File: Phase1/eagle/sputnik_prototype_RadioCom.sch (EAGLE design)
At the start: 98 parts, among them X1 332-44, Y1 32MHz

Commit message: Added more LEDs, filled in LNA values except one inductor which I still need to figure out
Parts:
- added LED7, LED8: (no value), psas_c3_team05:LED-0603
- added R11, R12: 1k, rcl_custom:R-US_0603-B-NOSILK
- C23: value (none) -> 1nF
- C24: value (none) -> 10nF
- C43: value (none) -> 100uF
- L8: value (none) -> 150nH
- R1: value (none) -> 250
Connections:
- removed net N$28: LED5.A
- new net N$21: LED7.K, R11.2
- new net N$33: LED8.K, R12.2
- net GND: now also R11.1, R12.1
- net PTC1: now also LED5.A
- net PTC3: now also LED7.A
- net PTC4: now also LED8.A
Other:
- note added: "TODO: FIGURE OUT VALUE FOR L7"
- note removed: "TODO: FIGURE OUT VALUES FOR LNA"
- moved on the sheet: JP2, LED1, LED4, LED5, LED6, R10, R4, R8, R9

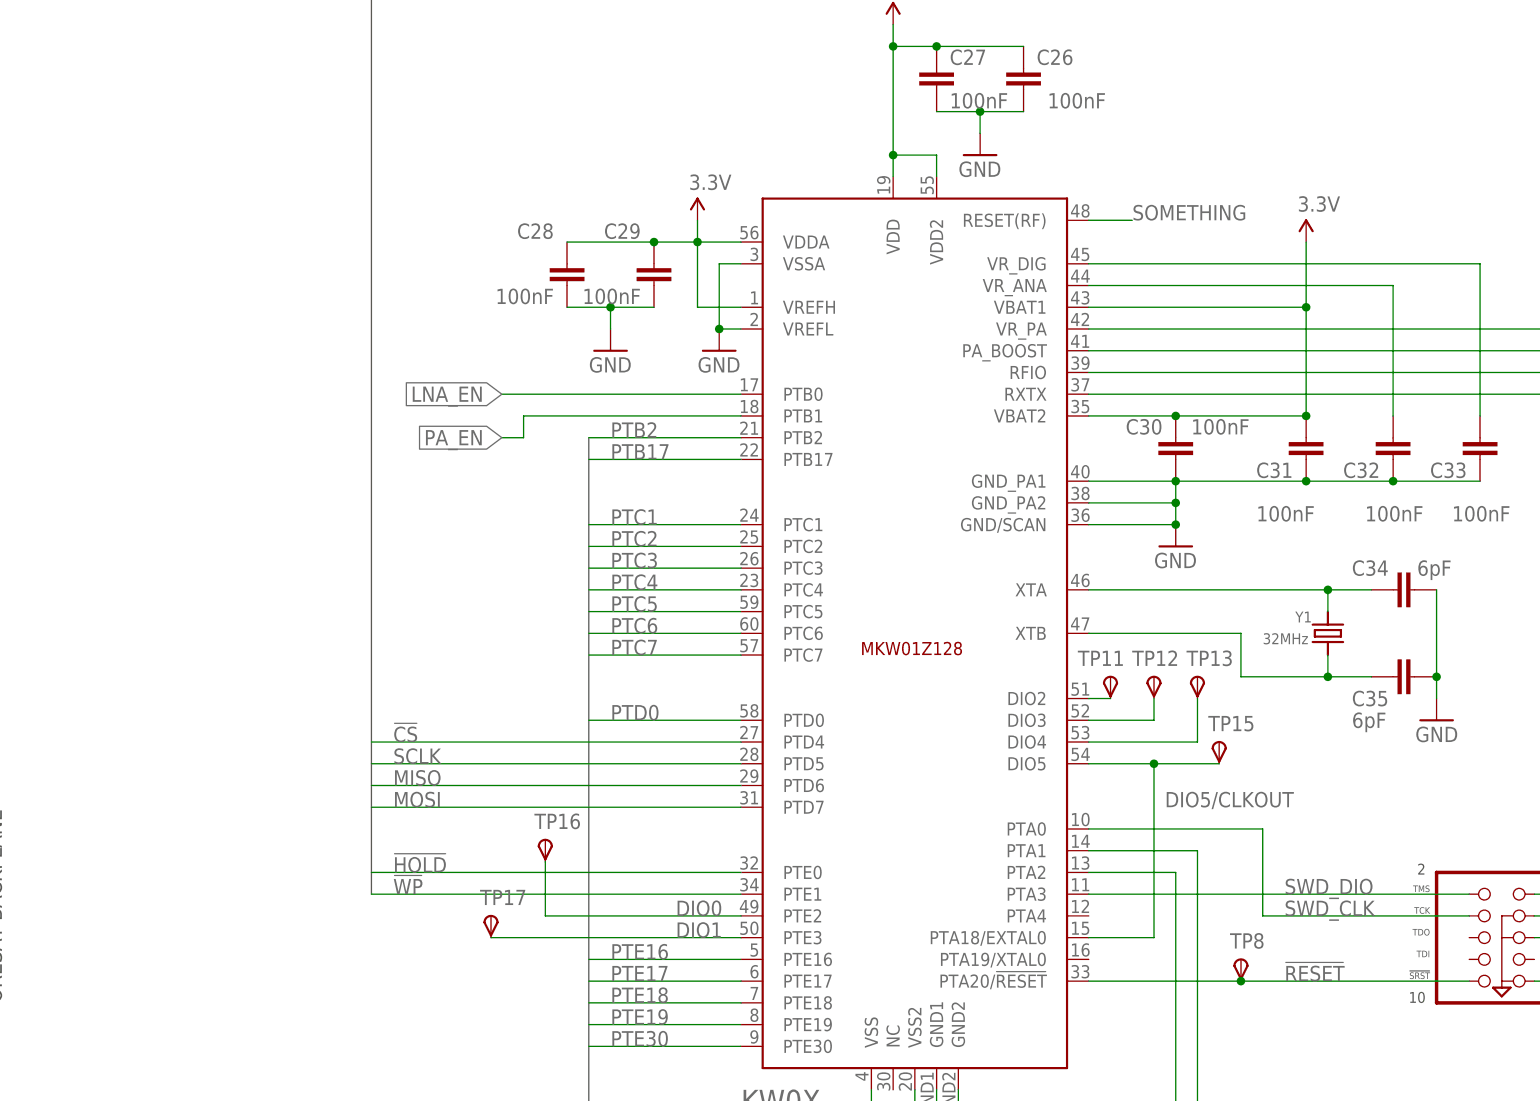
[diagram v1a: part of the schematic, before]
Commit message: Added RESET (RF) line to PTE2 GPIO. Waiting on LNA component values from MAACOM.
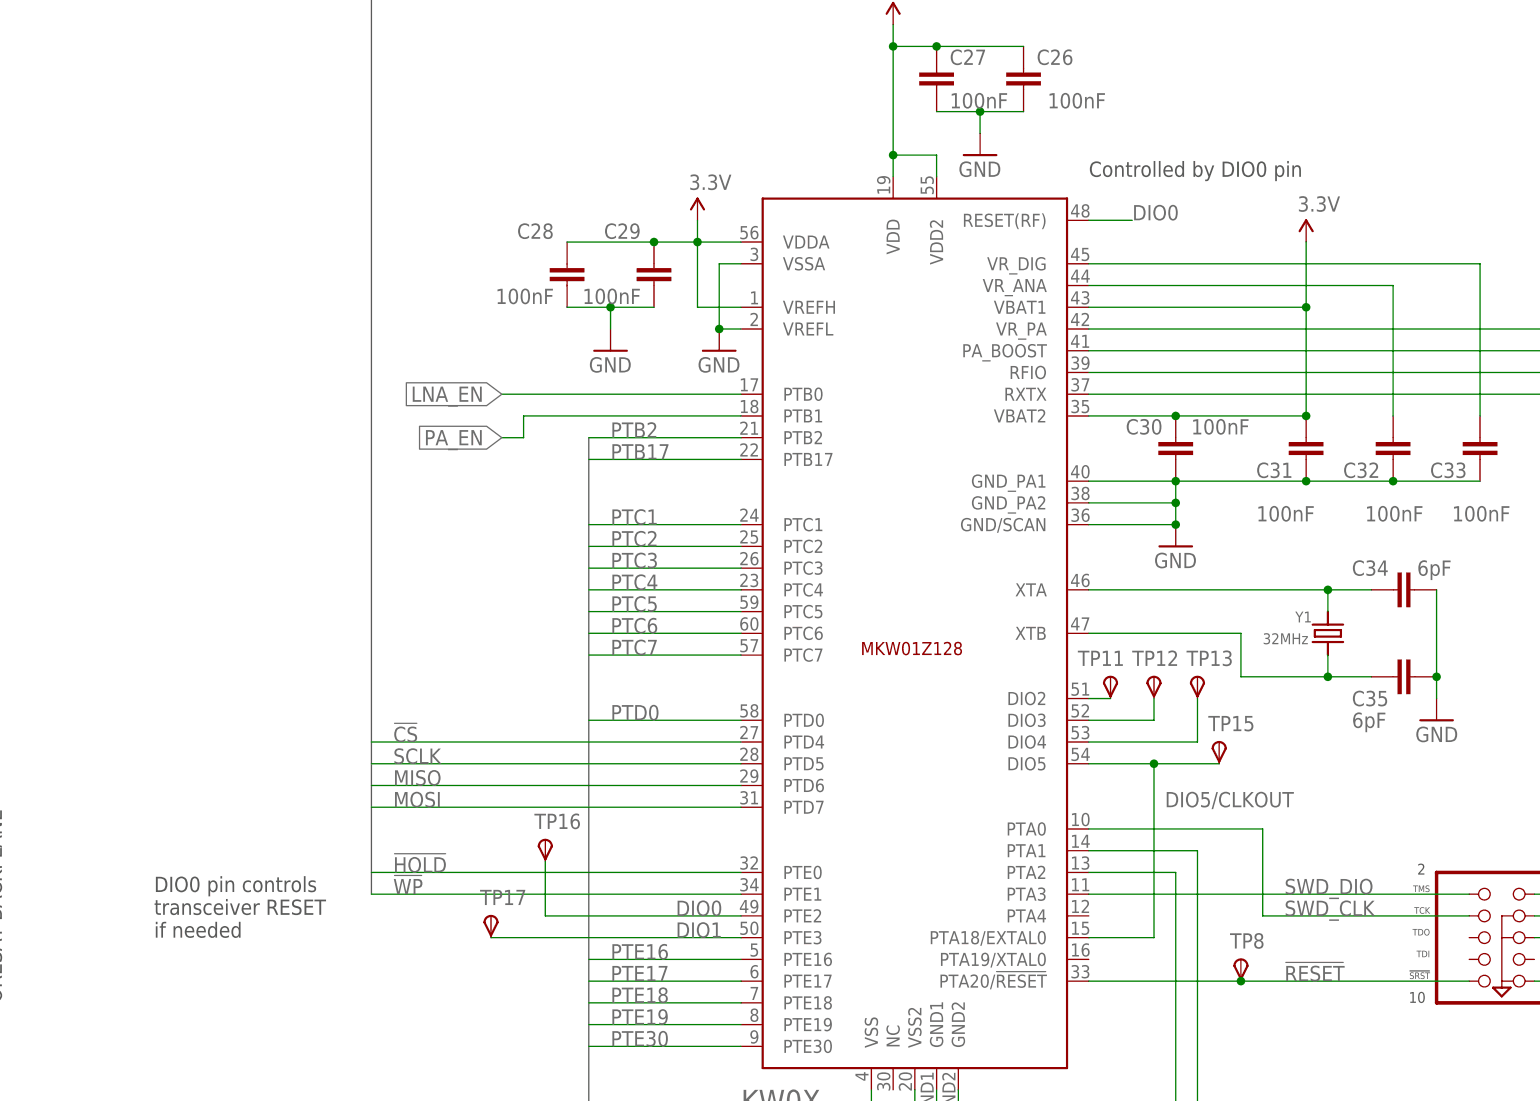
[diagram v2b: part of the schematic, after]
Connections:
- removed net SOMETHING: KW0X.RESET(RF)
- net DIO0: now also KW0X.RESET(RF)
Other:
- note added: "Controlled by DIO0 pin"
- note added: "DIO0 pin controls transceiver RESET if needed"
- note removed: "DOES !RESET NEED A PULL-UP?!"
- note removed: "FIXME!!!!"
- note removed: "TODO: -Make footprint for 22pin (83B-44PA-2DS(71)-ND) (H123075-ND)"
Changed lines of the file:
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@@
 <wire x1="83.82" y1="279.4" x2="139.7" y2="279.4" width="0.1524" layer="97" style="longdash"/>
 <wire x1="139.7" y1="279.4" x2="139.7" y2="322.58" width="0.1524" layer="97" style="longdash"/>
-<text x="104.14" y="66.04" size="1.778" layer="100">TODO:
--Make footprint for 22pin (83B-44PA-2DS(71)-ND)
-(H123075-ND)</text>
 <wire x1="314.96" y1="231.14" x2="241.3" y2="231.14" width="0.1524" layer="97" style="longdash"/>
 <wire x1="309.88" y1="99.06" x2="340.36" y2="99.06" width="0.1524" layer="97" style="longdash"/>
@@
 <wire x1="309.88" y1="78.74" x2="309.88" y2="99.06" width="0.1524" layer="97" style="longdash"/>
 <text x="312.42" y="96.52" size="1.778" layer="97">RF/DC GND connection</text>
-<text x="142.24" y="250.19" size="1.778" layer="100">FIXME!!!!</text>
-<text x="152.4" y="147.32" size="1.778" layer="100">DOES !RESET NEED
-A PULL-UP?!</text>
 <text x="213.36" y="86.36" size="1.778" layer="97">Debug interface</text>
 <wire x1="261.62" y1="2.54" x2="160.02" y2="2.54" width="0.1524" layer="97" style="longdash"/>
@@
 <text x="223.52" y="49.53" size="1.778" layer="97" rot="R90">Placed by access edge</text>
 <text x="7.62" y="154.94" size="1.778" layer="97" rot="R90">ORESAT BACKPLANE</text>
+<text x="134.62" y="251.46" size="1.778" layer="97">Controlled by DIO0 pin</text>
+<text x="25.4" y="162.56" size="1.778" layer="97">DIO0 pin controls
+transceiver RESET
+if needed</text>
 </plain>
 <instances>
@@
 </segment>
 </net>
-<net name="SOMETHING" class="0">
-<segment>
-<pinref part="KW0X" gate="G$1" pin="RESET(RF)"/>
-<wire x1="134.62" y1="246.38" x2="139.7" y2="246.38" width="0.1524" layer="91"/>
-<label x="139.7" y="246.38" size="1.778" layer="95"/>
-</segment>
-</net>
 <net name="LNA_EN" class="0">
 <segment>
@@
 <label x="86.36" y="165.1" size="1.778" layer="95"/>
 </segment>
-</net>
+<segment>
+<pinref part="KW0X" gate="G$1" pin="RESET(RF)"/>
+<wire x1="134.62" y1="246.38" x2="139.7" y2="246.38" width="0.1524" layer="91"/>
+<label x="139.7" y="246.38" size="1.778" layer="95"/>
+</segment>
+</net>

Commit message: OCD fixes on SPI flash. Made single nets on GPIO that aren't connected. Made new connectors for OreSat connector and RF connector and added them. Updates to a library part for the outline. Made it 4 layers, because that's what it's gonna be. Ooo the excitement, this is starting to look like a thing. Still waiting for final placement data from Jeremy before the connectors can be finalized.
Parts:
- removed SMA: SMAJ716-ND, psas_c3_team05:SMAJ716-ND
- removed X1: 332-44, con-garry:332-44
- added CF1: ORESAT-CONNECTOR-40PIN, oresat-eagle:ORESAT-CONNECTOR-40PIN
- added CF2: CON-MCX-LINX, oresat-eagle:CON-MCX-LINX
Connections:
- net !WP renamed PTE1
- removed net 3.3V1: LED2.A
- removed net N$32: LED6.A
- new net PTE0: KW0X.PTE0
- net !HOLD: no longer KW0X.PTE0
- net 3.3V: no longer TP5.PP
- net GND: now also CF1.37, CF1.38, CF1.39, CF1.40, CF2.SHIELD; no longer SMA.OUTERCONDUCTOR, X1-21.S, X1-22.S
- net N$11: now also TP5.PP
- net N$30: now also CF2.CENTER; no longer SMA.CENTERCONDUCTOR
- net PTB17: now also CF1.2; no longer X1-4.S
- net PTB2: now also CF1.1; no longer X1-3.S
- net PTC1: now also CF1.3; no longer X1-5.S
- net PTC2: now also CF1.4, LED6.A; no longer X1-6.S
- net PTC3: now also CF1.5; no longer X1-7.S
- net PTC4: now also CF1.6; no longer X1-8.S
- net PTC5: now also CF1.7; no longer X1-9.S
- net PTC6: now also CF1.8; no longer X1-10.S
- net PTC7: now also CF1.9; no longer X1-11.S
- net PTD0: now also CF1.10; no longer X1-12.S
- net PTE16: now also CF1.11; no longer X1-13.S
- net PTE17: now also CF1.12; no longer X1-14.S
- net PTE18: now also CF1.13; no longer X1-15.S
- net PTE19: now also CF1.14; no longer X1-16.S
- net UART0_RX: now also CF1.17, CF1.18; no longer X1-19.S, X1-20.S
- net UART0_TX: now also CF1.15, CF1.16; no longer X1-17.S, X1-18.S
- net V+: now also CF1.33, CF1.34, CF1.35, CF1.36; no longer X1-1.S, X1-2.S
- net VBIAS: now also LED2.A
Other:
- note removed: "UART connection between KW0x and ATMega128 PTA1 = KW0x UART0 RX PTA2 = KW0x UART0 TX PE1 = ATMega128 UART0 TX PE0 = ATMega128 UART0 RX PE1 is connected to PTA1 PE0 is connected to PTA2"
- moved on the sheet: C39, C40, C41, R2, R3, R5, TP10, TP14, TP5, TP6, TP7

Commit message: Uhh.... I did stuff? Fixed something? I can't remember. Found another NC on the KW0x.
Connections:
- new net PTA19: KW0X.PTA19/XTAL0
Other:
- note removed: "Controlled by DIO0 pin"
- moved on the sheet: TP16, TP17
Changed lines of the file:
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@@
 <text x="223.52" y="49.53" size="1.778" layer="97" rot="R90">Placed by access edge</text>
 <text x="7.62" y="154.94" size="1.778" layer="97" rot="R90">ORESAT BACKPLANE</text>
-<text x="134.62" y="251.46" size="1.778" layer="97">Controlled by DIO0 pin</text>
-<text x="25.4" y="162.56" size="1.778" layer="97">DIO0 pin controls
+<text x="140.97" y="257.81" size="1.778" layer="97">DIO0 pin controls
 transceiver RESET
 if needed</text>
@@
 <attribute name="TP_SIGNAL_NAME" x="148.59" y="191.77" size="1.778" layer="97"/>
 </instance>
-<instance part="TP16" gate="G$1" x="71.12" y="173.99"/>
-<instance part="TP17" gate="G$1" x="64.77" y="165.1"/>
+<instance part="TP16" gate="G$1" x="71.12" y="167.64"/>
+<instance part="TP17" gate="G$1" x="66.04" y="170.18"/>
 <instance part="R2" gate="R" x="88.9" y="314.96" rot="R90"/>
 <instance part="P+8" gate="G$1" x="88.9" y="322.58" rot="MR0"/>
@@
 <net name="DIO0" class="0">
 <segment>
+<pinref part="KW0X" gate="G$1" pin="RESET(RF)"/>
+<wire x1="134.62" y1="246.38" x2="139.7" y2="246.38" width="0.1524" layer="91"/>
+<wire x1="139.7" y1="246.38" x2="139.7" y2="276.86" width="0.1524" layer="91"/>
+<wire x1="139.7" y1="276.86" x2="43.18" y2="276.86" width="0.1524" layer="91"/>
+<wire x1="43.18" y1="276.86" x2="43.18" y2="165.1" width="0.1524" layer="91"/>
 <pinref part="KW0X" gate="G$1" pin="PTE2"/>
 <pinref part="TP16" gate="G$1" pin="PP"/>
 <wire x1="93.98" y1="165.1" x2="71.12" y2="165.1" width="0.1524" layer="91"/>
-<wire x1="71.12" y1="165.1" x2="71.12" y2="171.45" width="0.1524" layer="91"/>
 <label x="86.36" y="165.1" size="1.778" layer="95"/>
-</segment>
-<segment>
-<pinref part="KW0X" gate="G$1" pin="RESET(RF)"/>
-<wire x1="134.62" y1="246.38" x2="139.7" y2="246.38" width="0.1524" layer="91"/>
-<label x="139.7" y="246.38" size="1.778" layer="95"/>
+<wire x1="43.18" y1="165.1" x2="71.12" y2="165.1" width="0.1524" layer="91"/>
+<junction x="71.12" y="165.1"/>
 </segment>
 </net>
@@
 <pinref part="TP17" gate="G$1" pin="PP"/>
 <pinref part="KW0X" gate="G$1" pin="PTE3"/>
-<wire x1="93.98" y1="162.56" x2="64.77" y2="162.56" width="0.1524" layer="91"/>
+<wire x1="93.98" y1="162.56" x2="66.04" y2="162.56" width="0.1524" layer="91"/>
+<wire x1="66.04" y1="162.56" x2="66.04" y2="167.64" width="0.1524" layer="91"/>
 <label x="86.36" y="162.56" size="1.778" layer="95"/>
 </segment>
@@
 </segment>
 </net>
+<net name="PTA19" class="0">
+<segment>
+<pinref part="KW0X" gate="G$1" pin="PTA19/XTAL0"/>
+<wire x1="134.62" y1="160.02" x2="142.24" y2="160.02" width="0.1524" layer="91"/>
+</segment>
+</net>

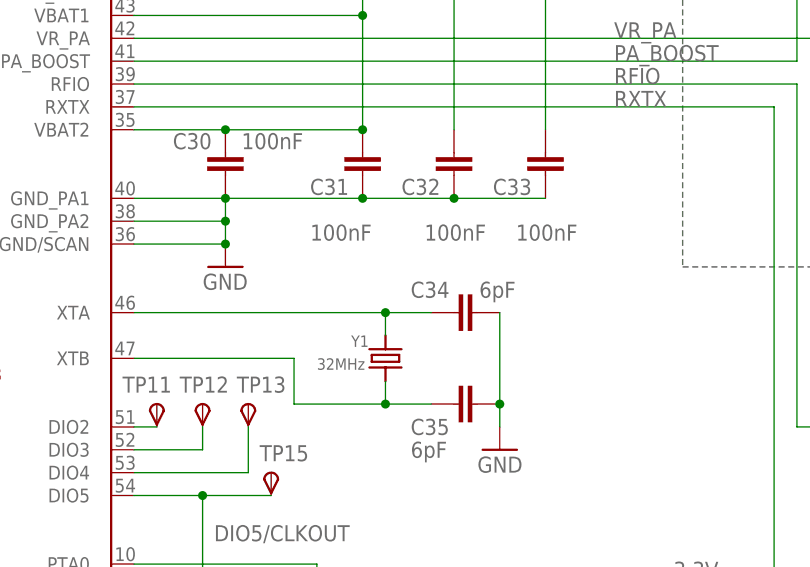
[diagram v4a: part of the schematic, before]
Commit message: Added crystal test point, started layout setup
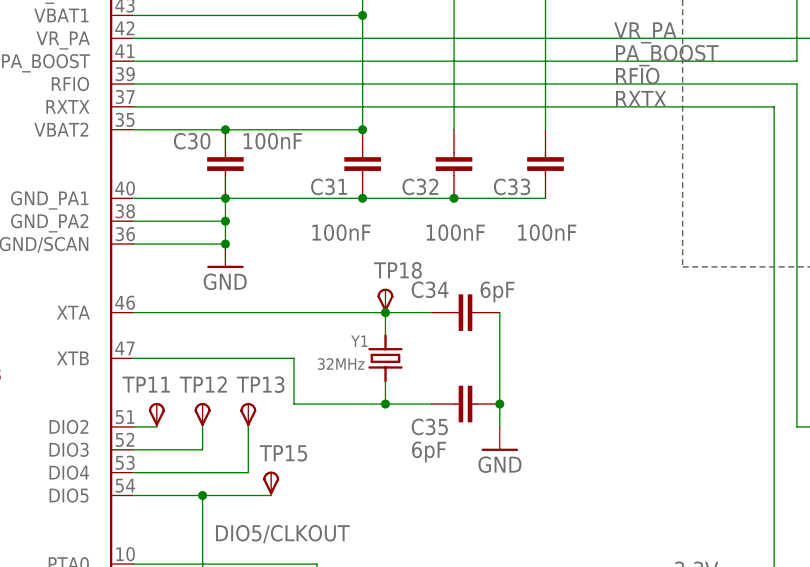
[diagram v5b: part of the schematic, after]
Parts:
- added TP18: TPSPAD1-13, testpad:TPSPAD1-13
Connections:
- net N$6: now also TP18.PP
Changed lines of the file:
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@@
 <?xml version="1.0" encoding="utf-8"?>
 <!DOCTYPE eagle SYSTEM "eagle.dtd">
-<eagle version="7.3.0">
+<eagle version="7.4.0">
 <drawing>
 <settings>
@@
 <setting verticaltext="up"/>
 </settings>
-<grid distance="0.05" unitdist="inch" unit="inch" style="lines" multiple="2" display="yes" altdistance="0.01" altunitdist="inch" altunit="inch"/>
+<grid distance="0.1" unitdist="inch" unit="inch" style="lines" multiple="1" display="no" altdistance="0.01" altunitdist="inch" altunit="inch"/>
 <layers>
 <layer number="1" name="Top" color="4" fill="1" visible="no" active="no"/>
@@
 <part name="CF1" library="oresat-eagle" deviceset="ORESAT-CONNECTOR-40PIN" device=""/>
 <part name="CF2" library="oresat-eagle" deviceset="CON-MCX-LINX" device=""/>
+<part name="TP18" library="testpad" deviceset="TPS" device="PAD1-13"/>
 </parts>
 <sheets>
@@
 <attribute name="VALUE" x="511.81" y="168.91" size="1.27" layer="95"/>
 </instance>
+<instance part="TP18" gate="G$1" x="162.56" y="205.74" smashed="yes">
+<attribute name="NAME" x="161.29" y="207.01" size="1.778" layer="95"/>
+<attribute name="TP_SIGNAL_NAME" x="163.83" y="204.47" size="1.778" layer="97"/>
+</instance>
 </instances>
 <busses>
@@
 <wire x1="162.56" y1="200.66" x2="162.56" y2="203.2" width="0.1524" layer="91"/>
 <junction x="162.56" y="203.2"/>
-</segment>
-</net>
+<pinref part="TP18" gate="G$1" pin="PP"/>
+</segment>
+</net>

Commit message: Poor Jake. It's like there's some crazy guy screwing with him every time he commits... oh, wait. Huh. Anyway. Updated board outline with keepouts. Moved connectors into position and locked. Added shield over LNA (how could this be a bad idea? maybe the PA could use a sheild too, but with heat sinking?). Uncrossed the streams: make sure your main RF lines never, ever dive through the board. That sucks, keep it to one layer. So I had to move the PA and LNA around. Still needs some cleanup, but it's OK. Put resistors for sensitive supplies by the supplies, so no stray low impedance leakage.
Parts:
- removed TP6, TP7: TPSPAD1-13, testpad:TPSPAD1-13
- added SH1: BMI-S-202-SHIELD, hw-laird-bmi-s-202:BMI-S-202-SHIELD
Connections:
- removed net N$26: LED5.K, R9.2
- removed net N$29: LED6.K, R10.2
- removed net N$33: LED8.K, R12.2
- new net N$23: LED8.A, R12.1
- new net V_LNA_FILTERED: LED2.A, R6.1
- new net V_PA_FILTERED: LED3.A, R7.1
- net 3.3V: now also R8.2; no longer LED4.A
- net GND: now also LED1.K, LED2.K, LED3.K, LED4.K, LED5.K, LED6.K, LED7.K, LED8.K, SH1.P$1; no longer R10.1, R11.1, R12.1, R4.1, R6.1, R7.1, R8.1, R9.1
- net LNA_IN: now also TRSWITCH.RF3; no longer TRSWITCH.RF2
- net N$14: now also LED1.A, R4.1; no longer LED1.K, R4.2
- net N$15: now also LED5.A, R9.1; no longer LED2.K, R6.2
- net N$2: now also TRSWITCH.RF2; no longer TRSWITCH.RF3
- net N$20: now also LED6.A, R10.1; no longer LED3.K, R7.2
- net N$21: now also LED7.A, R11.1; no longer LED7.K, R11.2
- net N$22: now also LED4.A, R8.1; no longer LED4.K, R8.2
- net PTC1: now also R9.2; no longer LED5.A
- net PTC2: now also R10.2; no longer LED6.A
- net PTC3: now also R11.2; no longer LED7.A
- net PTC4: now also R12.2; no longer LED8.A
- net UART0_RX: no longer TP6.PP
- net UART0_TX: no longer TP7.PP
- net V+: now also R4.2; no longer LED1.A
- net VBIAS: now also R6.2; no longer LED2.A
- net VPA: now also R7.2; no longer LED3.A
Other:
- moved on the sheet: LED1, LED2, LED3, LED4, LED5, LED6, LED7, LED8, R10, R11, R12, R4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
